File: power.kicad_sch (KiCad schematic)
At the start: 110 parts, among them U1 LT8350RV#PBF, U2 MP2386GG, U3 TPS65983BAZBHR

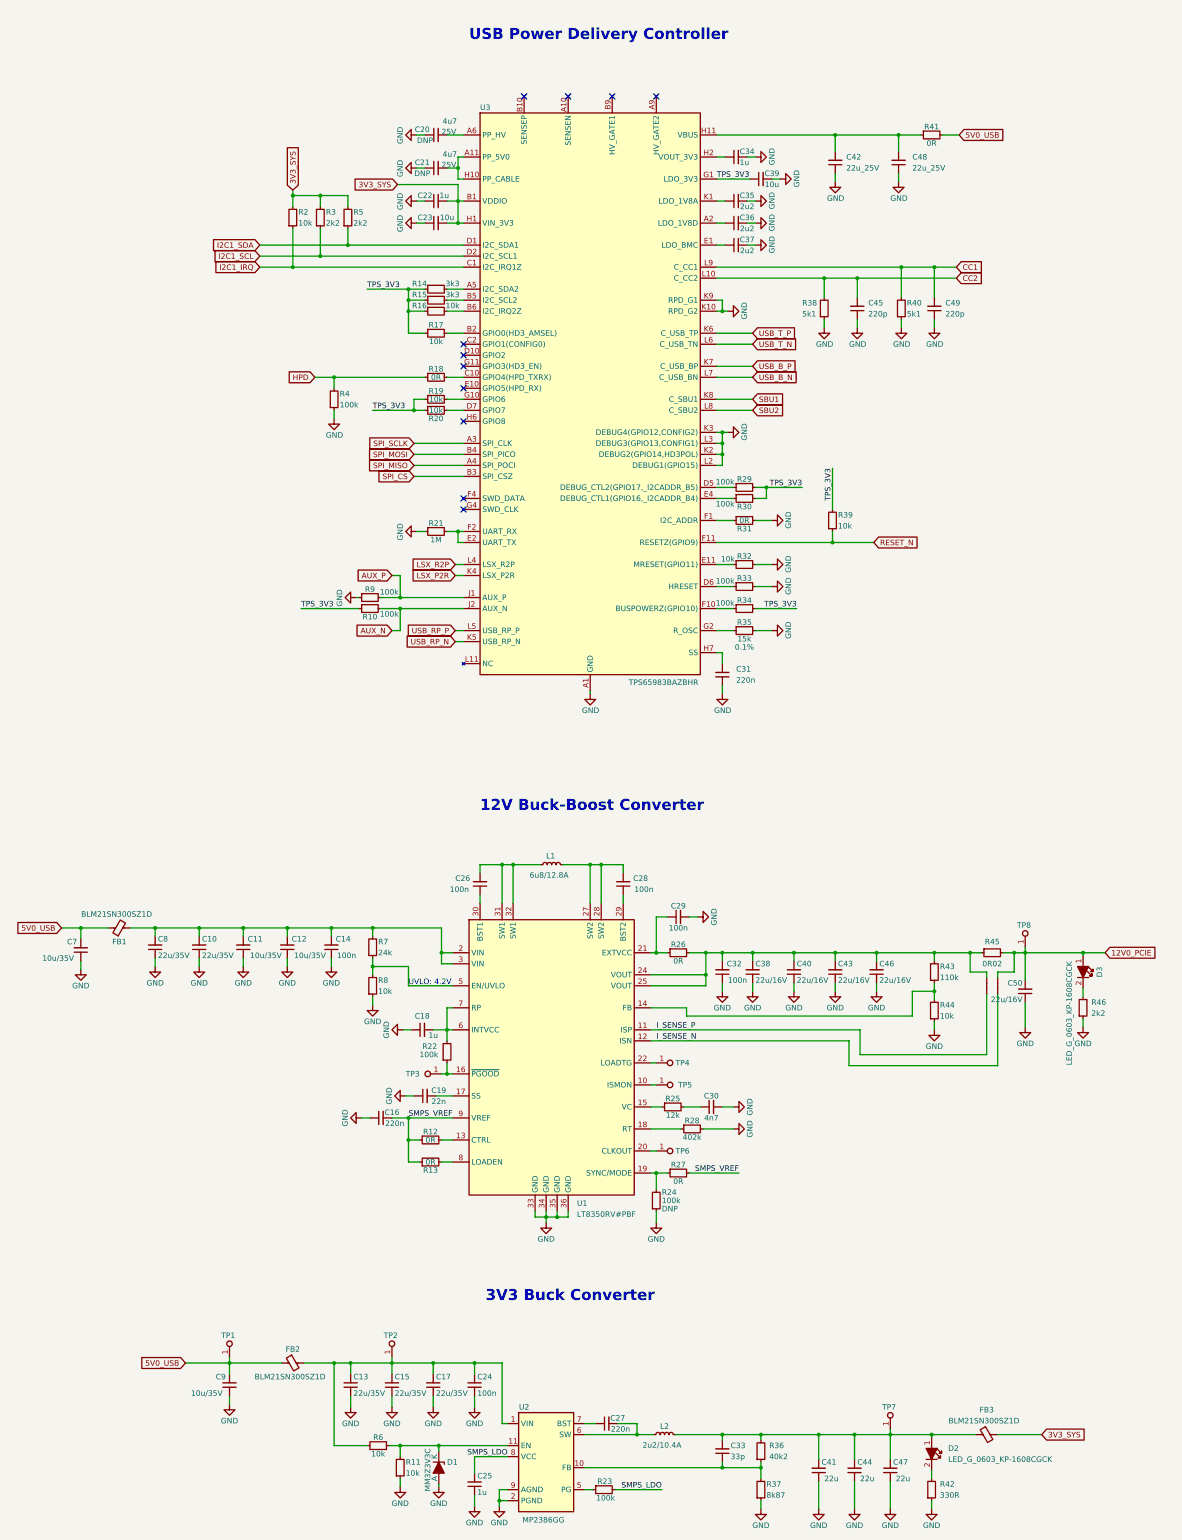
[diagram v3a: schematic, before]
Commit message: Added molex connector and power managment circuity for +12V power rails
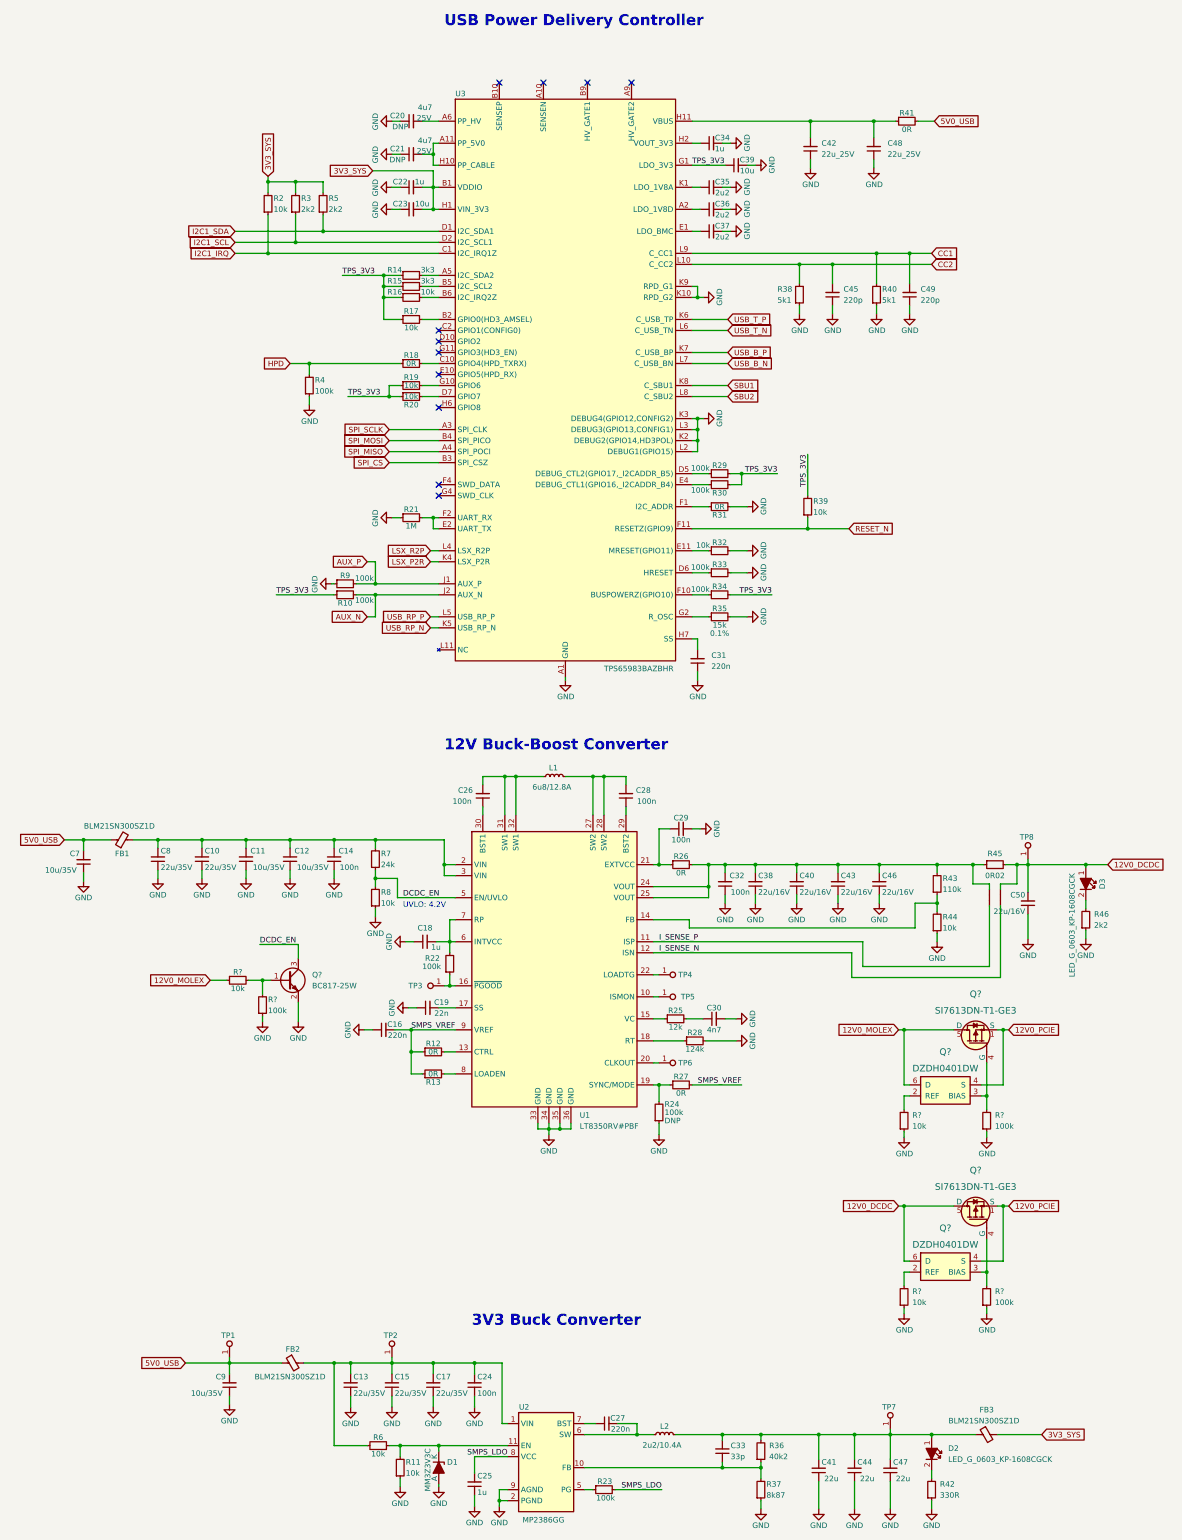
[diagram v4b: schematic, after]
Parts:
- removed R28: R_402k_0402, antmicro-footprints:R_0402_1005Metric, symbol antmicroResistors0402:R_402k_0402
- added Q? (x2): DZDH0401DW, antmicro-footprints:SOT-363, symbol antmicroPMICORControllersIdealDiodes:DZDH0401DW
- added Q?: BC817-25W, antmicro-footprints:SOT-323, symbol antmicroTransistorsBipolarSingle:BC817-25W
- added Q? (x2): SI7613DN-T1-GE3, antmicro-footprints:Vishay_PowerPAK_1212-8_Single, symbol antmicroTransistorsFETsMOSFETsSingle:SI7613DN-T1-GE3
- added R28: R_124k_0402, antmicro-footprints:R_0402_1005Metric, symbol antmicroResistors0402:R_124k_0402
- added R? (x3): R_100k_0402, antmicro-footprints:R_0402_1005Metric, symbol antmicroResistors0402:R_100k_0402
- added R? (x3): R_10k_0402, antmicro-footprints:R_0402_1005Metric, symbol antmicroResistors0402:R_10k_0402
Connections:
- net 12V0_PCIE: now also Q?.1 (S), Q?.1 (S), Q?.2 (S), Q?.2 (S), Q?.3 (S), Q?.3 (S), Q?.4 (S), Q?.4 (S); no longer C50.2, D3.1, R45.2, TP11.2, TP8.1
- net GND: now also Q?.2 (E), R28.2, R?.1, R?.1, R?.1, R?.1, R?.1
- net DCDC_EN: now reaches R7.1, R8.2, U1.5 (EN/UVLO)
- net DCDC_EN: now also Q?.3 (C)
- net at U1.18 (RT): now also R28.1
- new net: Q?.2 (REF), R?.2 (x2)
- new net: Q?.3 (BIAS), Q?.4 (G), R?.2 (x2)
- new net: Q?.1 (B), R?.2, R?.2
- new net 12V0_DCDC: C50.2, D3.1, Q?.5 (D), Q?.6 (D), R45.2, TP11.2, TP8.1
- new net 12V0_MOLEX: Q?.5 (D), Q?.6 (D), R?.1
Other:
- moved on the sheet: C10, C11, C12, C14, C16, C18, C19, C20, C21, C22, C23, C26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

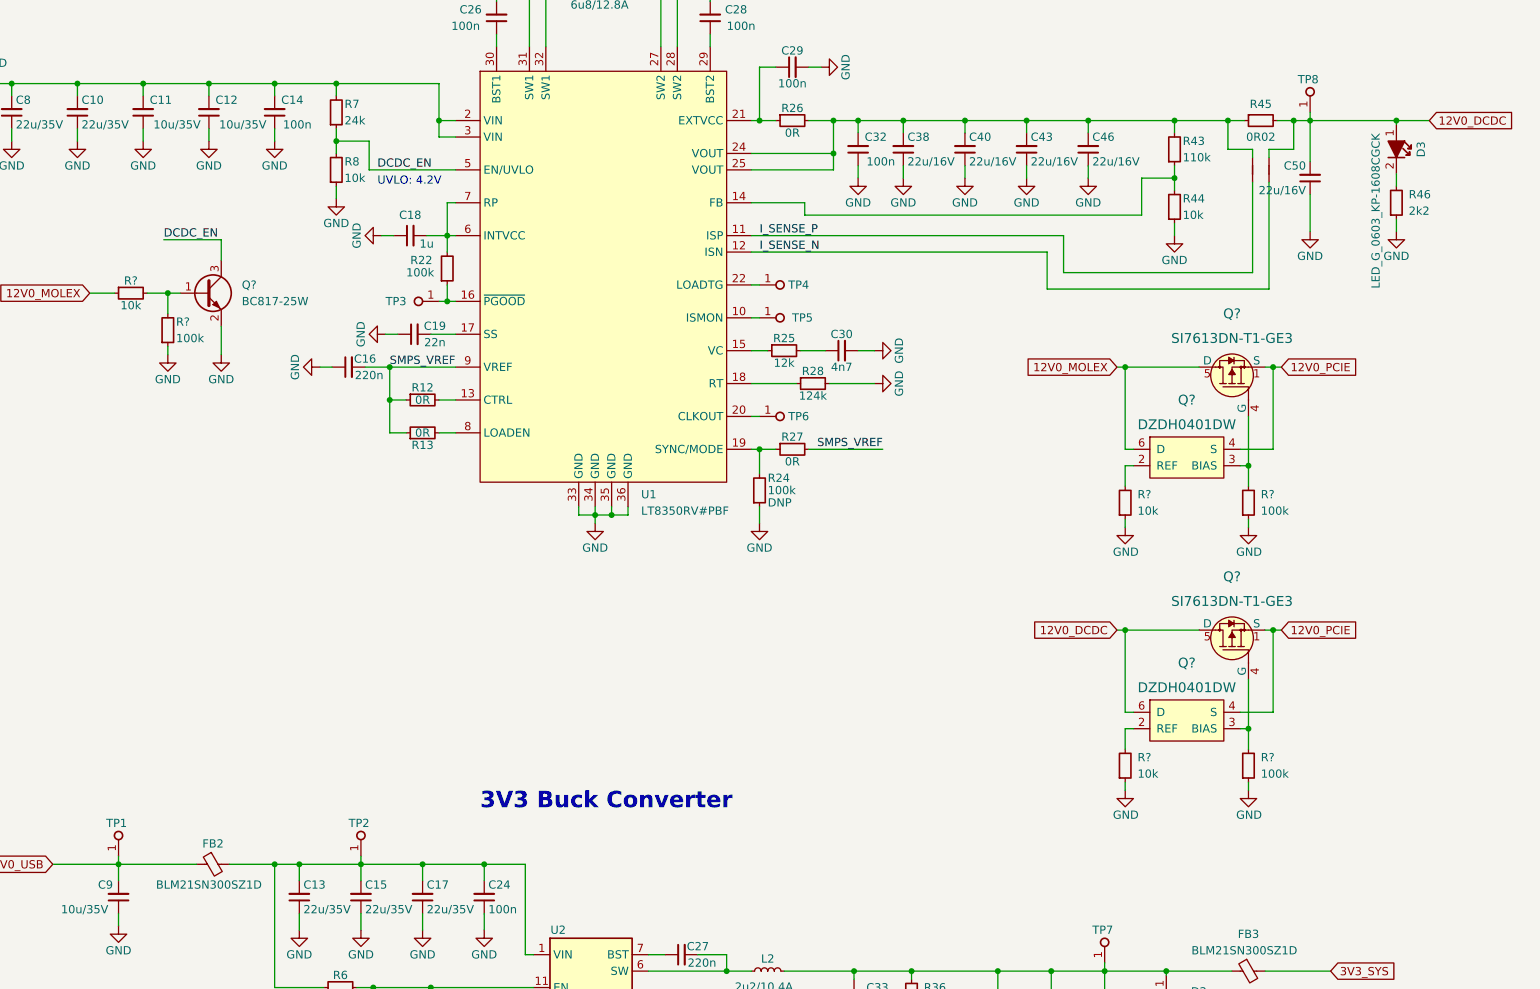
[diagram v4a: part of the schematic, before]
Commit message: Finished placement of molex connector and power management circuity for +12V rails, finished routing of all power planes
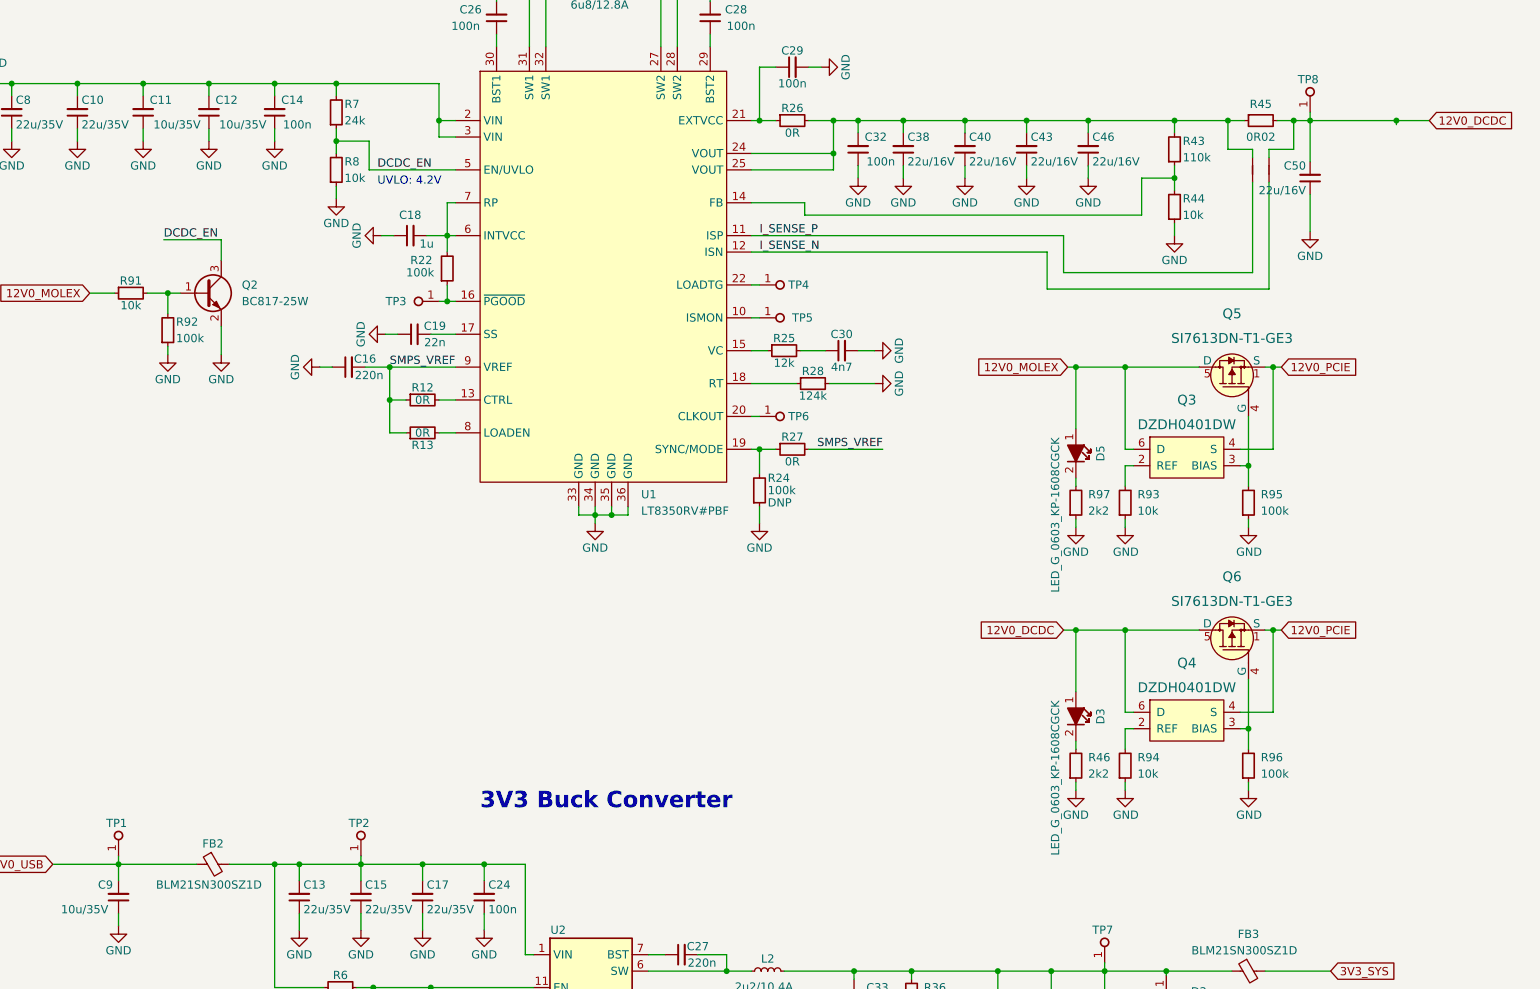
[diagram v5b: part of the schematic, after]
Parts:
- added D5: LED_G_0603_KP-1608CGCK, antmicro-footprints:LED_0603_1608Metric_G, symbol antmicroLEDIndicationDiscrete:LED_G_0603_KP-1608CGCK
- added R97: R_2k2_0402, antmicro-footprints:R_0402_1005Metric, symbol antmicroResistors0402:R_2k2_0402
- gave numbers to parts that had none: 11
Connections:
- net 12V0_MOLEX: now also D5.1
- net GND: now also R97.1
- new net: D5.2, R97.2
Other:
- moved on the sheet: D3, R46

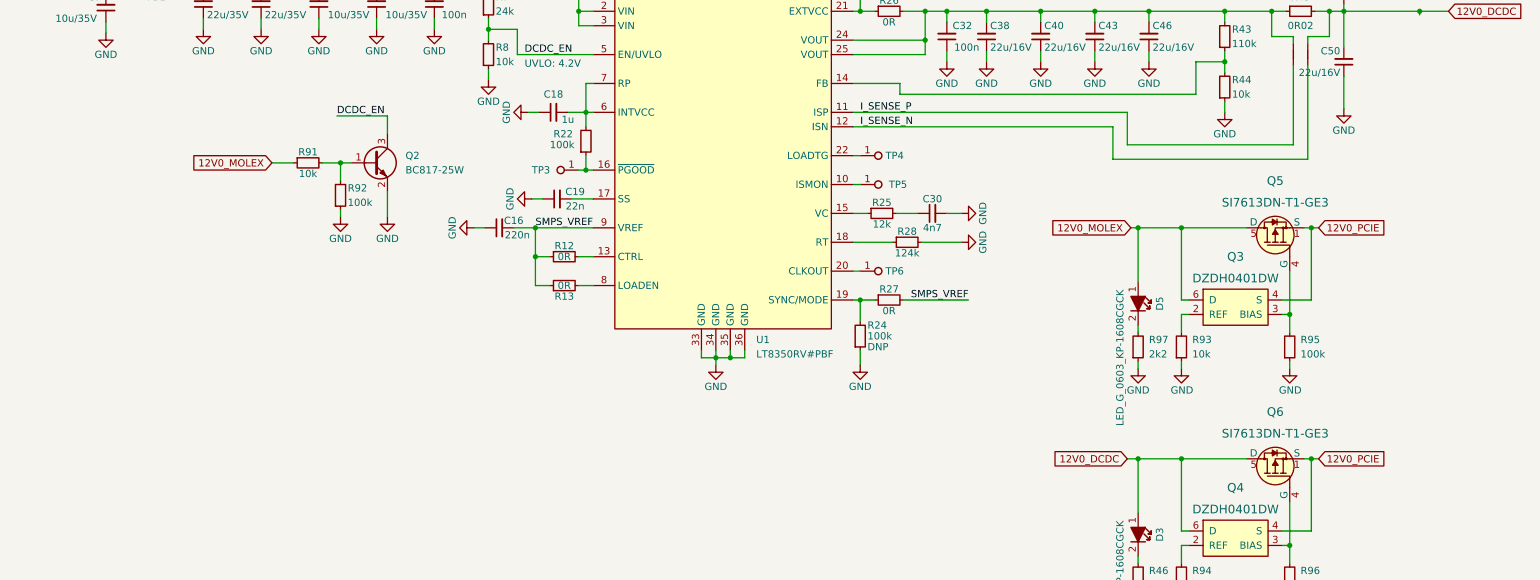
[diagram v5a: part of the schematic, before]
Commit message: Added capacitors for 12V input close to molex connector, added 0R between PCIe connector's 12V pads and ideal diodes output
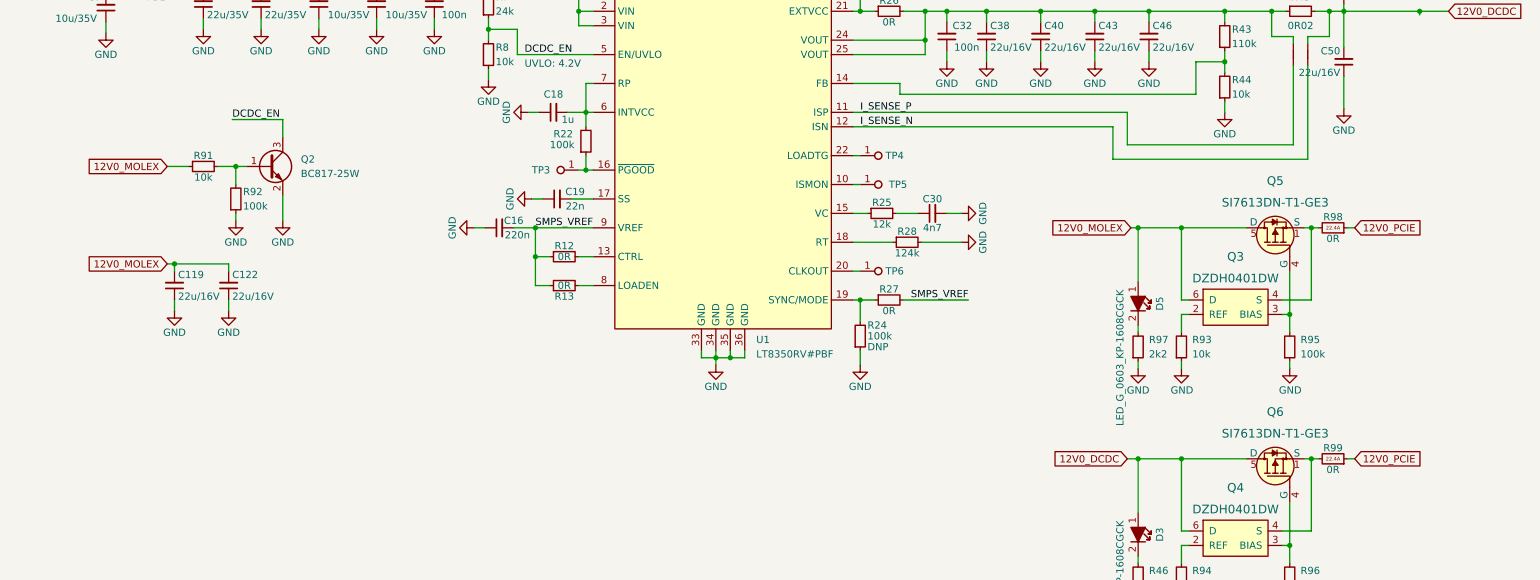
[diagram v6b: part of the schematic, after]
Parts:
- added C119, C122: C_22u_16V_0603, antmicro-footprints:C_0603_1608Metric, symbol antmicroCapacitors0603:C_22u_16V_0603
- added R98, R99: R_0R_22.4A_0603, antmicro-footprints:R_0603_1608Metric, symbol antmicroResistors0603:R_0R_22.4A_0603
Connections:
- net 12V0_MOLEX: now also C119.2, C122.2
- net 12V0_PCIE: now also R98.1, R99.1; no longer Q3.4 (S), Q4.4 (S), Q5.1 (S), Q5.2 (S), Q5.3 (S), Q6.1 (S), Q6.2 (S), Q6.3 (S)
- net GND: now also C119.1, C122.1
- new net: Q4.4 (S), Q6.1 (S), Q6.2 (S), Q6.3 (S), R99.2
- new net: Q3.4 (S), Q5.1 (S), Q5.2 (S), Q5.3 (S), R98.2
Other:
- moved on the sheet: Q2, R91, R92
